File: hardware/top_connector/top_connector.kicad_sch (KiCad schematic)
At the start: 13 parts, among them J1 to prev top connector, J2 to next top connector, J3 to module, U1 XL1509-5.0, U2 74LVC1G66

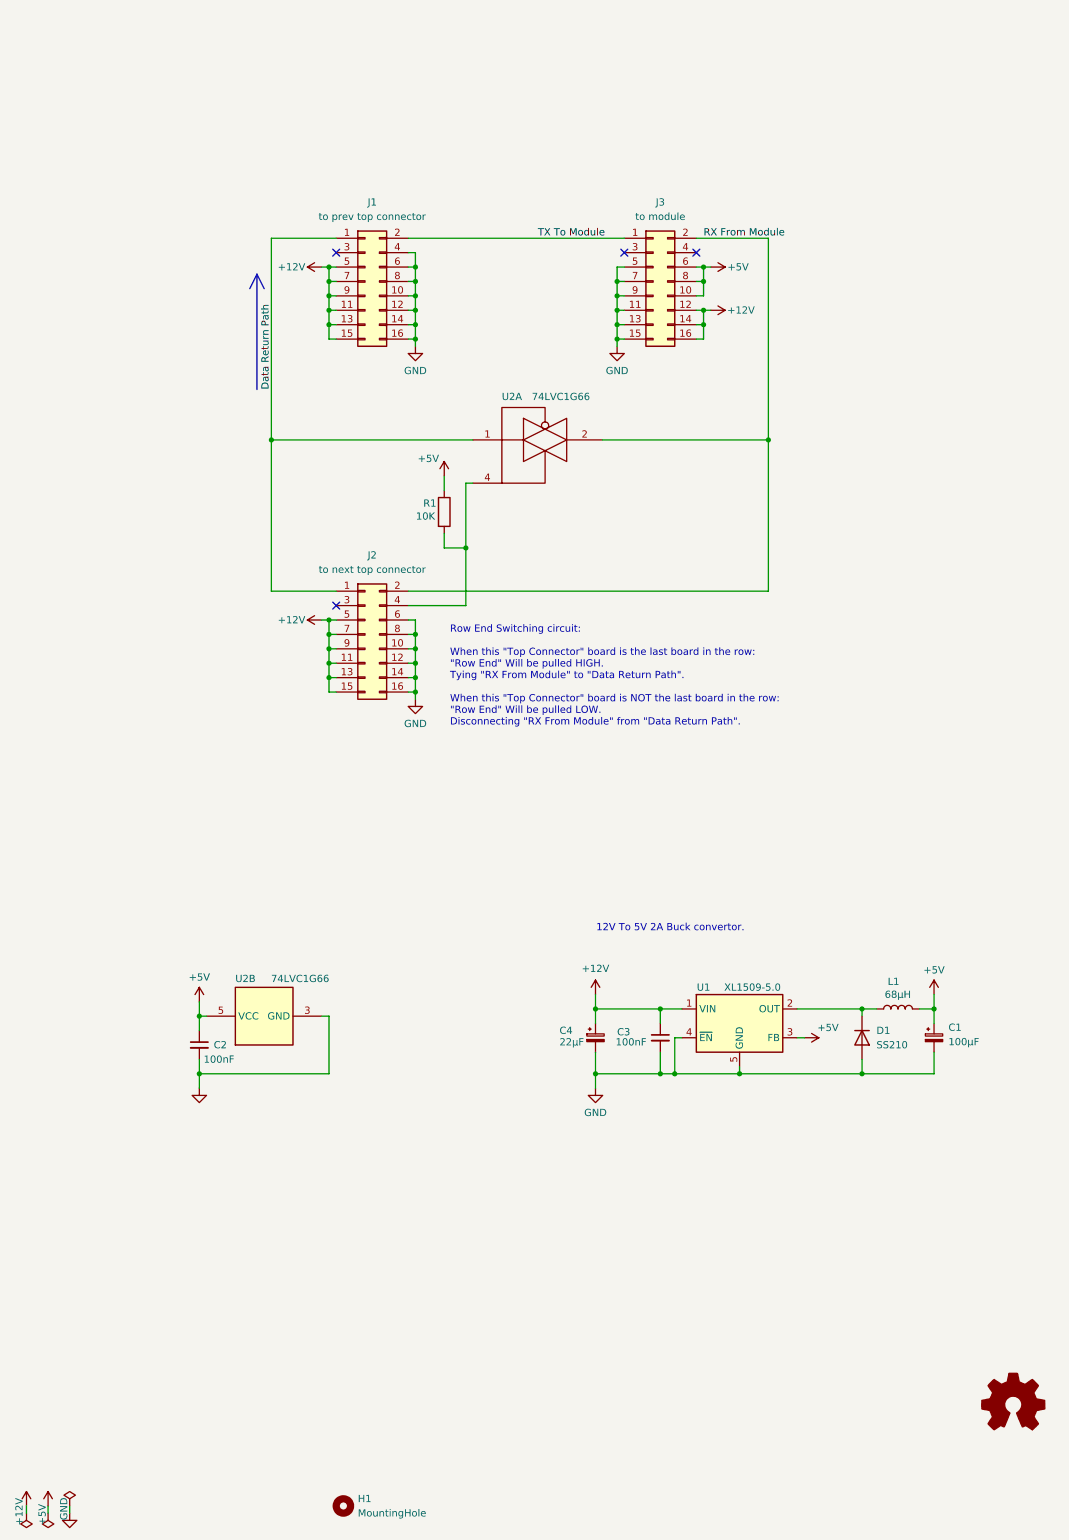
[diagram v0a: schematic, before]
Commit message: Switching to KiCad: Added side panel schematic and board
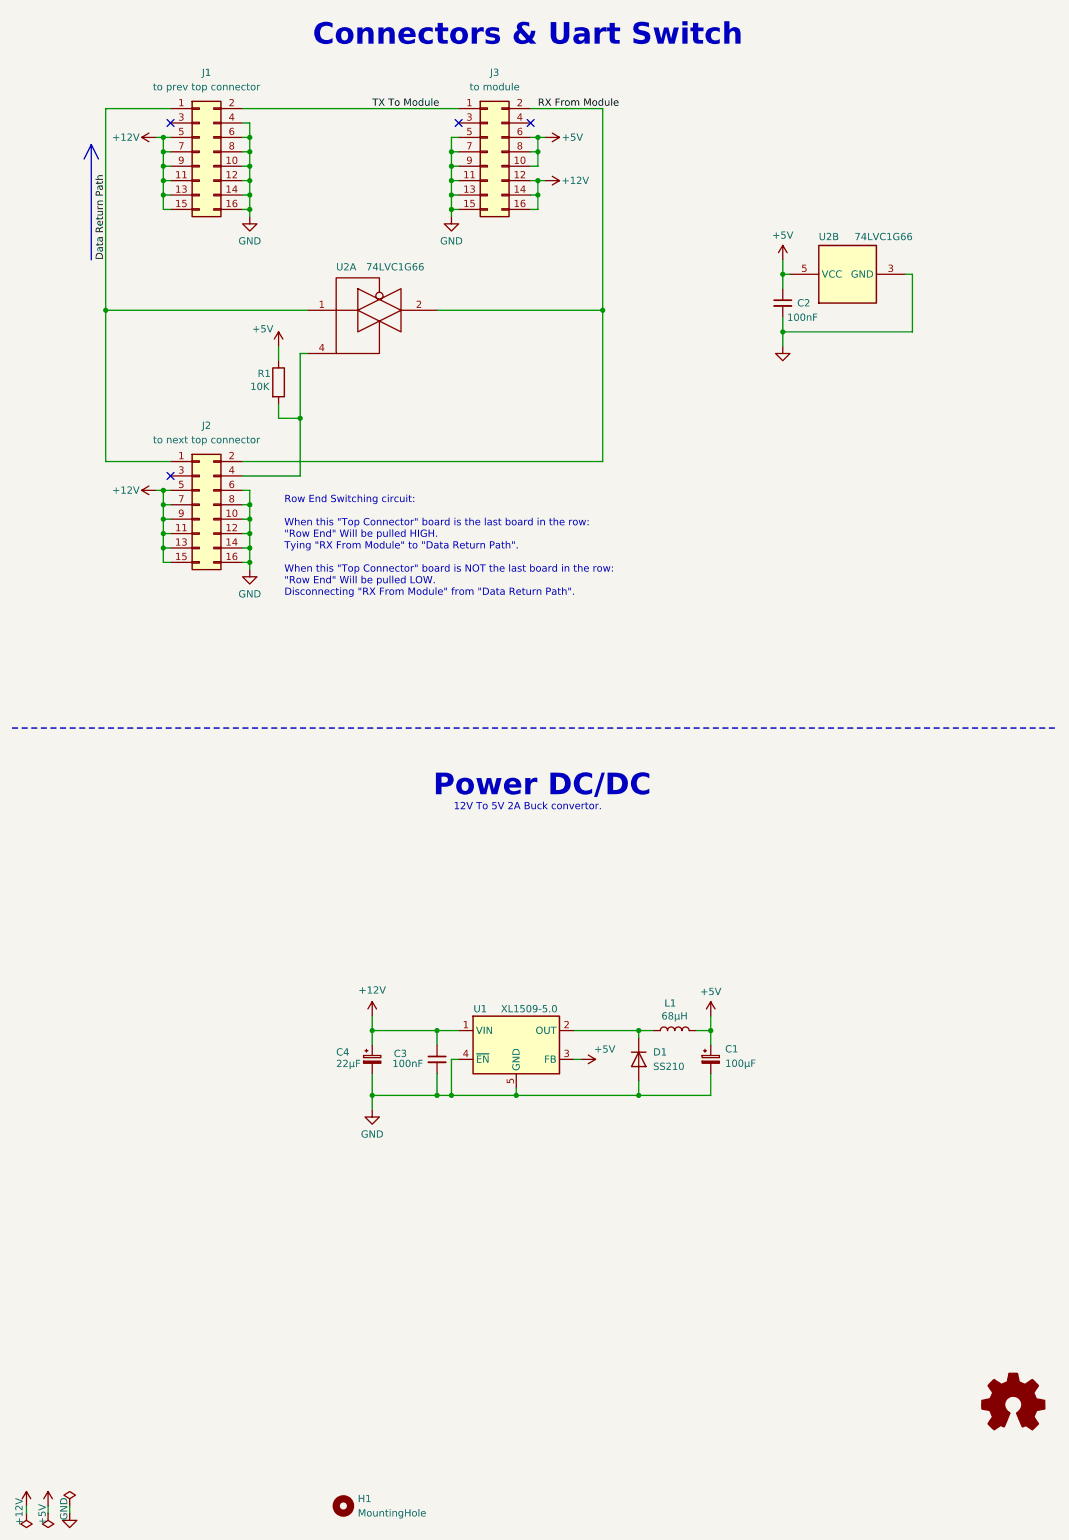
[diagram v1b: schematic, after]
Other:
- note added: "Connectors & Uart Switch"
- note added: "Power DC/DC"
- moved on the sheet: C1, C2, C3, C4, D1, J1, J2, J3, L1, R1, U1, U2A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
